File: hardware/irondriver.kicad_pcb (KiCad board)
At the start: 2 copper layers, 70 x 60 mm, 75 parts, among them P1 CONN_01X02, P2 CONN_01X02, P3 CONN_02X07, P6 CONN_01X03, Q1 MMBT3906, Q2 MMBT3904, Q3 MMBT3904, U1 STM32F103C8T6, U2 LM2596, U3 AD8606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

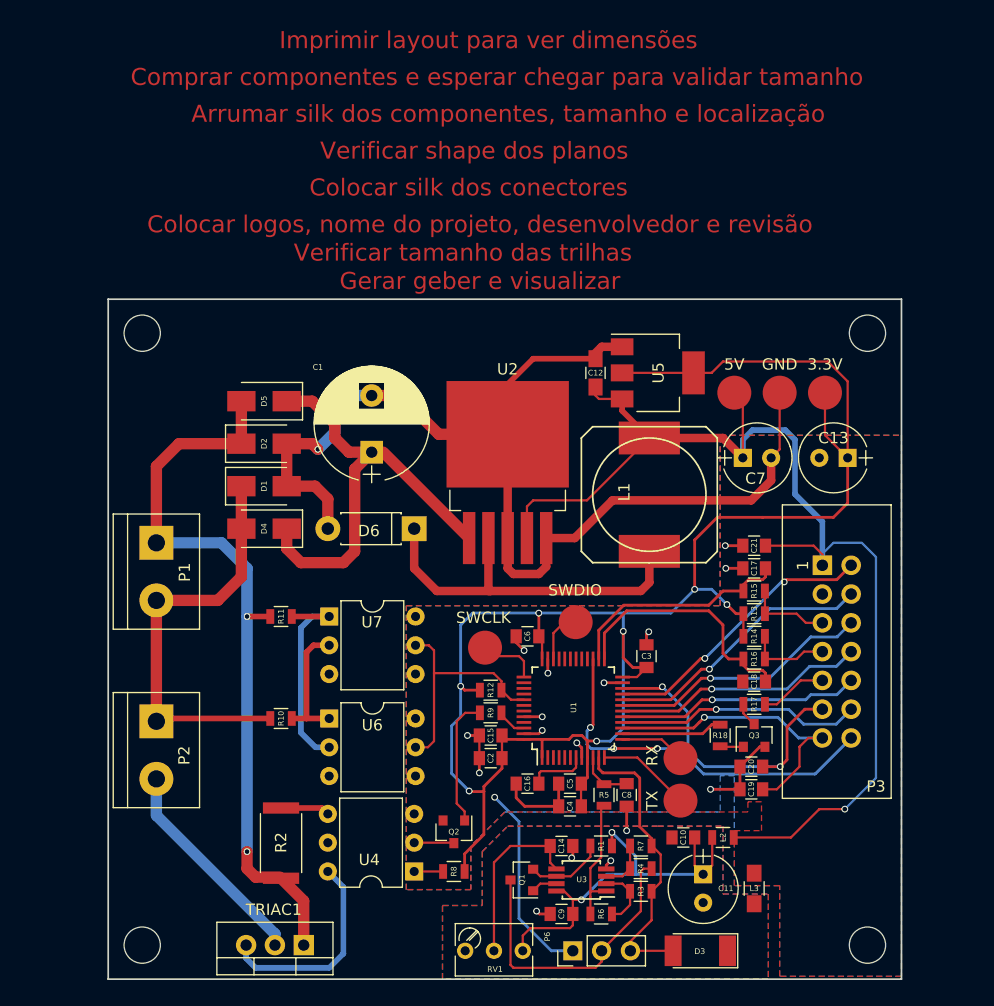
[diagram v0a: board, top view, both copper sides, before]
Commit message: Changed silk placement and size. Added logo and author information.
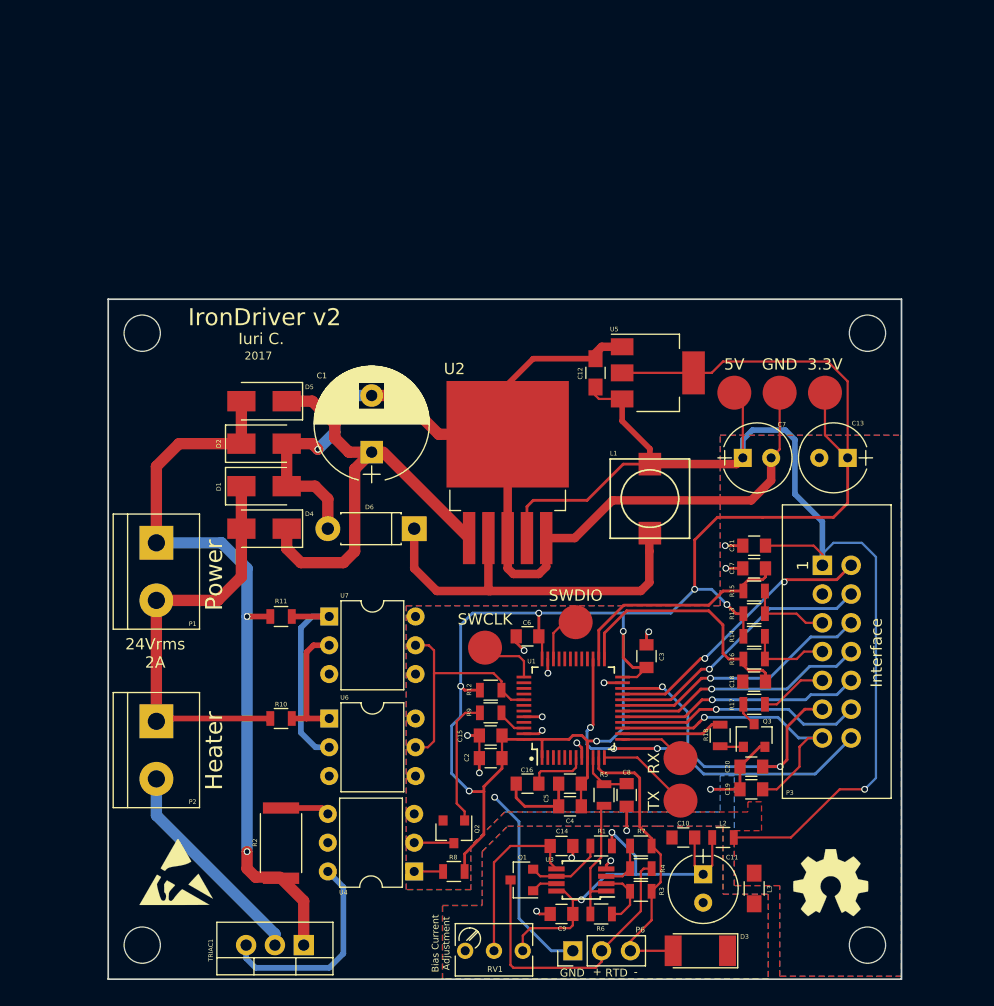
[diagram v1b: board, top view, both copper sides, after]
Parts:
- added REF***: OSHW-Symbol_6.7x6mm_SilkScreen, Symbols:OSHW-Symbol_6.7x6mm_SilkScreen, F.Cu at (113.8, 141.5)
- added REF***: ESD-Logo_6.6x6mm_SilkScreen, Symbols:ESD-Logo_6.6x6mm_SilkScreen, F.Cu at (56.0, 140.5)
- L1: footprint Inductors:SELF-WE-PD-XXL -> SELF-WE-1mH
- moved L1 0.35 mm to (97.8, 107.6)
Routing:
- net Net-(D6-Pad1): track 33.0 -> 34.6 mm
- net +5VD: track 105.0 -> 105.8 mm
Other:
- board text added: "+"
- board text added: "-"
- board text added: "2017"
- board text added: "24Vrms 2A"
- board text added: "Bias Current Adjustment"
- board text added: "GND"
- board text added: "Heater"
- board text added: "Interface"
- board text added: "IronDriver v2"
- board text added: "Iuri C."
- board text added: "Power"
- board text added: "RTD"
- board text removed: "Arrumar silk dos componentes, tamanho e localização"
- board text removed: "Colocar logos, nome do projeto, desenvolvedor e revisão"
- board text removed: "Colocar silk dos conectores"
- board text removed: "Comprar componentes e esperar chegar para validar tamanho"
- board text removed: "Gerar geber e visualizar"
- board text removed: "Imprimir layout para ver dimensões"
- board text removed: "Verificar shape dos planos"
- board text removed: "Verificar tamanho das trilhas"
